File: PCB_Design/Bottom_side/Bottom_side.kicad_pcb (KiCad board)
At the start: 2 copper layers, 95.2 x 94 mm, 146 parts, among them Q1 Q_NMOS_GSD, Q2 Q_NMOS_GSD, Q3 Q_NMOS_GSD, Q4 Q_NMOS_GSD, Q5 Q_PMOS_GSD, Q6 Q_PMOS_GSD, Q7 Q_PMOS_GSD, Q8 Q_NMOS_GSD, Q9 Q_NMOS_GSD, U1 MAX668, U2 MAX668, U3 MAX668, U4 MCP4728, U5 TPS54302, U6 TPS54302

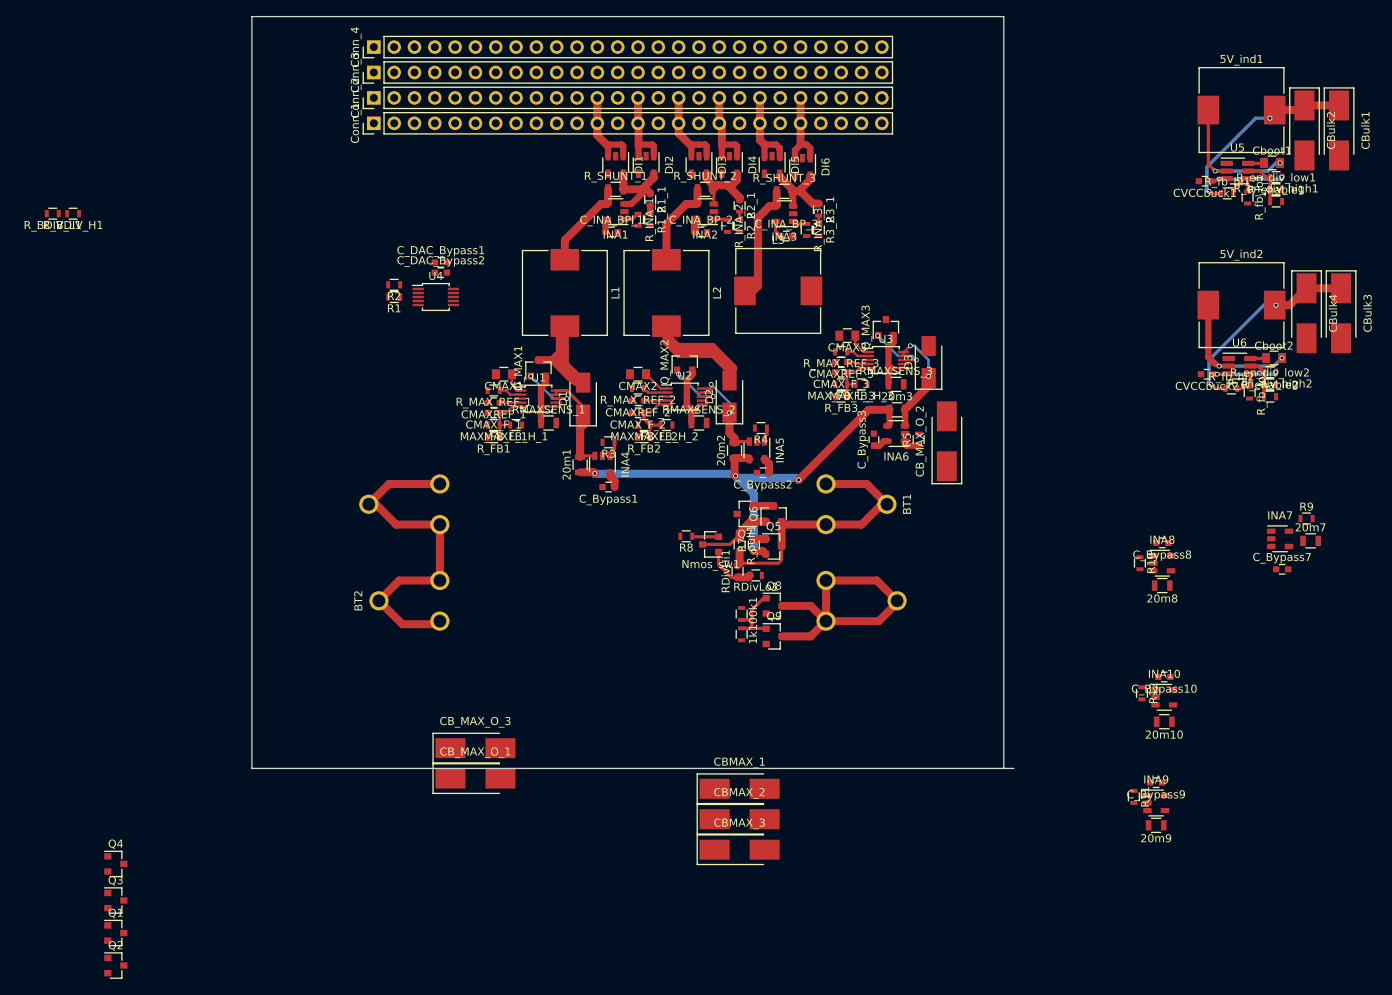
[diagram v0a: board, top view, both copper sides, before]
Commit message: PCB bottom layer populated
PCB bottom layer populated, and waiting for top layer to be merged.
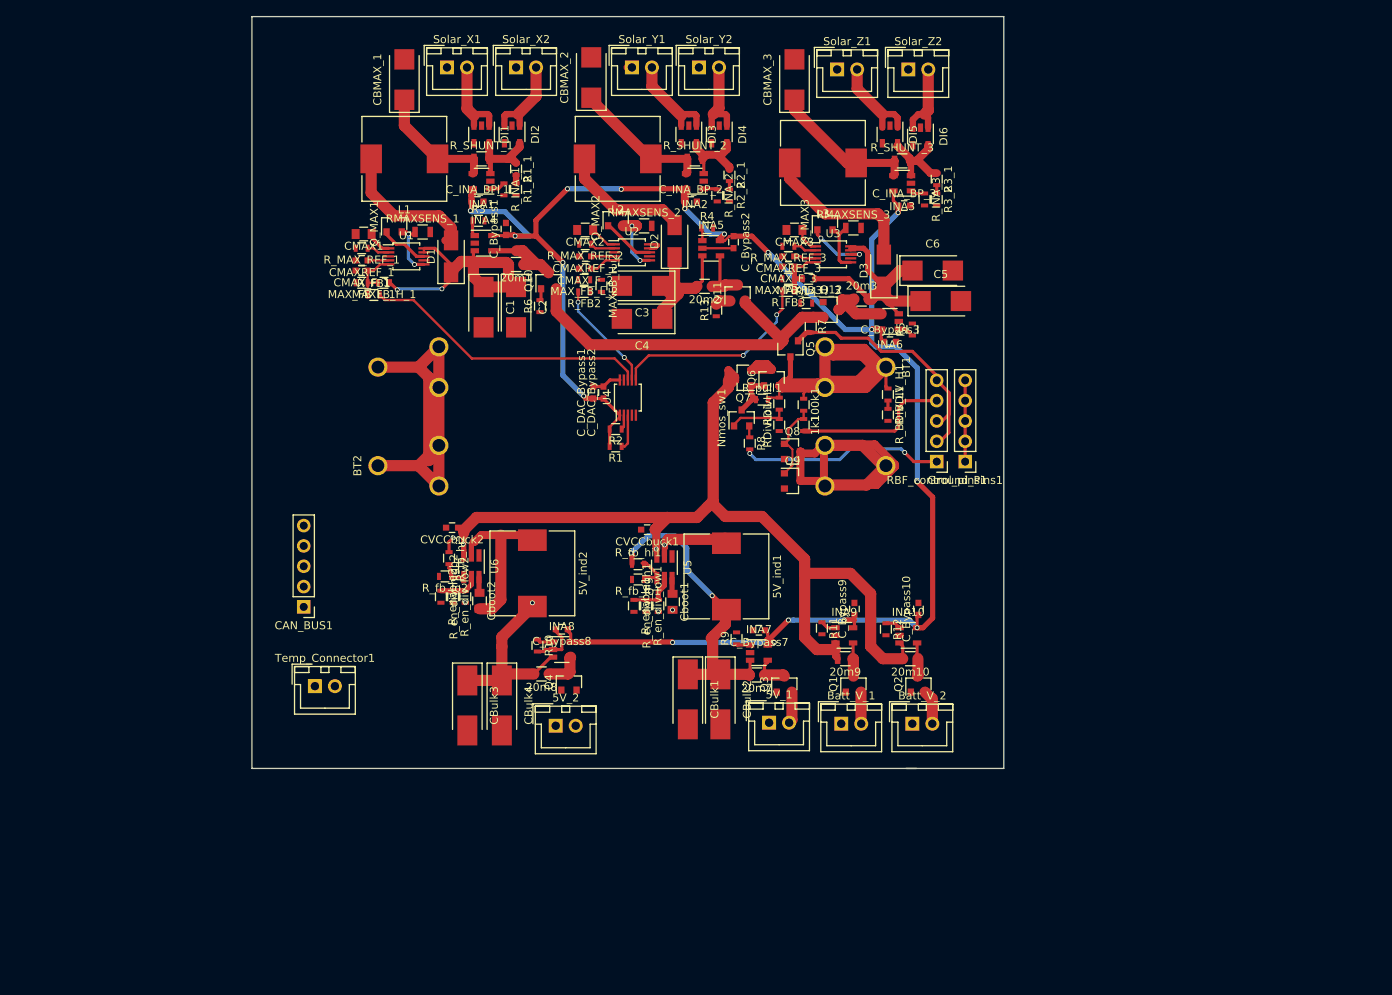
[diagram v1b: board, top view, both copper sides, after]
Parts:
- removed CB_MAX_O_1, CB_MAX_O_2, CB_MAX_O_3: 68uF, Capacitors_Tantalum_SMD:CP_Tantalum_Case-C_EIA-6032-28_Hand
- removed Conn_1, Conn_3: Conn_01x26, Socket_Strips:Socket_Strip_Straight_1x26_Pitch2.54mm
- removed Conn_2: Conn_2, Socket_Strips:Socket_Strip_Straight_1x26_Pitch2.54mm
- removed Conn_4: Conn_4, Socket_Strips:Socket_Strip_Straight_1x26_Pitch2.54mm
- added 5V_1: Jst_Conn, Connectors_JST:JST_XH_B02B-XH-A_02x2.50mm_Straight, F.Cu at (116.7, 123.8)
- added 5V_2: Jst_Conn, Connectors_JST:JST_XH_B02B-XH-A_02x2.50mm_Straight, F.Cu at (90.0, 124.2)
- added Batt_V_1: Jst_Conn, Connectors_JST:JST_XH_B02B-XH-A_02x2.50mm_Straight, F.Cu at (125.7, 124.0)
- added Batt_V_2: Jst_Conn, Connectors_JST:JST_XH_B02B-XH-A_02x2.50mm_Straight, F.Cu at (134.6, 124.0)
- added C1: CP, Capacitors_Tantalum_SMD:CP_Tantalum_Case-C_EIA-6032-28_Reflow, F.Cu at (81.0, 71.9)
- added C2: CP, Capacitors_Tantalum_SMD:CP_Tantalum_Case-C_EIA-6032-28_Reflow, F.Cu at (85.1, 71.9)
- added C3: CP, Capacitors_Tantalum_SMD:CP_Tantalum_Case-C_EIA-6032-28_Reflow, F.Cu at (100.8, 69.2)
- added C4: CP, Capacitors_Tantalum_SMD:CP_Tantalum_Case-C_EIA-6032-28_Reflow, F.Cu at (100.8, 73.3)
- added C5: CP, Capacitors_Tantalum_SMD:CP_Tantalum_Case-C_EIA-6032-28_Reflow, F.Cu at (138.2, 71.1)
- added C6: CP, Capacitors_Tantalum_SMD:CP_Tantalum_Case-C_EIA-6032-28_Reflow, F.Cu at (137.2, 67.3)
- added CAN_BUS1: 5_pin_2.56, Socket_Strips:Socket_Strip_Straight_1x05_Pitch2.54mm, F.Cu at (58.5, 109.3)
- added Ground_Pins1: 2.56_socket_male, Socket_Strips:Socket_Strip_Straight_1x05_Pitch2.54mm, F.Cu at (141.2, 91.2)
- added Q10: Q_PMOS_GSD, TO_SOT_Packages_SMD:SOT-23, F.Cu at (89.2, 68.6)
- added Q11: Q_PMOS_GSD, TO_SOT_Packages_SMD:SOT-23, F.Cu at (112.8, 70.1)
- added Q12: Q_PMOS_GSD, TO_SOT_Packages_SMD:SOT-23, F.Cu at (124.5, 72.2)
- added R13: 220k, Resistors_SMD:R_0603, F.Cu at (110.1, 72.3)
- added R14: 220k, Resistors_SMD:R_0603, F.Cu at (121.3, 71.4)
- added R6: 220k, Resistors_SMD:R_0603, F.Cu at (88.1, 71.8)
- added RBF_control_pins1: 5_pin_2.56, Socket_Strips:Socket_Strip_Straight_1x05_Pitch2.54mm, F.Cu at (137.7, 91.2)
- added Solar_X1: JST_Connector, Connectors_JST:JST_XH_B02B-XH-A_02x2.50mm_Straight, F.Cu at (76.5, 41.9)
- added Solar_X2: JST_Connector, Connectors_JST:JST_XH_B02B-XH-A_02x2.50mm_Straight, F.Cu at (85.1, 41.9)
- added Solar_Y1: JST_Connector, Connectors_JST:JST_XH_B02B-XH-A_02x2.50mm_Straight, F.Cu at (99.6, 41.9)
- added Solar_Y2: JST_Connector, Connectors_JST:JST_XH_B02B-XH-A_02x2.50mm_Straight, F.Cu at (108.0, 41.9)
- added Solar_Z1: JST_Connector, Connectors_JST:JST_XH_B02B-XH-A_02x2.50mm_Straight, F.Cu at (125.2, 42.2)
- added Solar_Z2: JST_Connector, Connectors_JST:JST_XH_B02B-XH-A_02x2.50mm_Straight, F.Cu at (134.1, 42.2)
- added Temp_Connector1: JST_conn, Connectors_JST:JST_XH_B02B-XH-A_02x2.50mm_Straight, F.Cu at (59.9, 119.3)
- BT1, BT2: footprint Batt_Hold:18650_Holder_FULL -> Battery_Holder_Lib:18650_Holder_FULL
- CBMAX_1, CBMAX_2, CBMAX_3: footprint Capacitors_Tantalum_SMD:CP_Tantalum_Case-C_EIA-6032-28_Hand -> Capacitors_Tantalum_SMD:CP_Tantalum_Case-C_EIA-6032-28_Reflow
- moved CBulk3 119.7 mm to (79.0, 121.7)
- moved CBulk4 111.9 mm to (83.3, 121.7)
- moved CBulk1 108.1 mm to (106.6, 120.9)
- moved R_BDIV_L1 107.4 mm to (131.6, 85.3), turned to 270 degrees
- moved R_enable2 106.6 mm to (75.7, 108.1), turned to 270 degrees
- moved Q2 106.3 mm to (135.4, 119.0), turned to 90 degrees
- moved R_en_div_low2 105.5 mm to (77.2, 108.1), turned to 270 degrees
- moved R_en_div_high2 104.4 mm to (78.7, 108.1), turned to 90 degrees
- moved R_BDIV_H1 104.3 mm to (131.6, 82.8), turned to 270 degrees
- moved Cboot2 103.8 mm to (80.5, 108.6), turned to 270 degrees
- moved R_fb_lo2 103.2 mm to (76.2, 105.5), turned to 180 degrees
- moved CBulk2 101.9 mm to (110.6, 120.9)
- moved R_fb_hi2 100.1 mm to (76.7, 103.3), turned to 270 degrees
- moved U6 99.2 mm to (79.5, 104.3), turned to 270 degrees
- moved CBMAX_1 98.1 mm to (71.1, 43.4), turned to 90 degrees
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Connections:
- net /Connectors/Ideal_Diodes/X+ renamed /Connectors And Inputs/Ideal_Diodes/X+
- net /Connectors/Ideal_Diodes/X- renamed /Connectors And Inputs/Ideal_Diodes/X-
- net /Connectors/Ideal_Diodes/Y+ renamed /Connectors And Inputs/Ideal_Diodes/Y+
- net /Connectors/Ideal_Diodes/Y- renamed /Connectors And Inputs/Ideal_Diodes/Y-
- net /Connectors/Ideal_Diodes/Z+ renamed /Connectors And Inputs/Ideal_Diodes/Z+
- net /Connectors/Ideal_Diodes/Z- renamed /Connectors And Inputs/Ideal_Diodes/Z-
- net /Input/InaOutput/INA_out/Ina_Analog renamed /Input/InaOutput/INA_out_2/Ina_Analog
- net /Input/LDAC renamed /LDAC
- net /Input/SCL renamed /SCL
- net /Input/SDA renamed /SDA
- 20m1 pad 1: /Input/Output_1 -> /Input/InaOutput/INA_out/I_out
- 20m10 pad 1: /OUTPUT/Sheet5A5E5DCD/I_out -> /OUTPUT/INA_BV_2/I_out
- 20m2 pad 1: /Input/Output_1 -> /Input/InaOutput/INA_out_2/I_out
- 20m3 pad 1: /Input/Output_1 -> /Input/InaOutput/INA_out_3/I_out
- 20m7 pad 1: /OUTPUT/Sheet5A5E5DCD/I_out -> /OUTPUT/Ina_5V_Out/I_out
- 20m7 pad 2: /OUTPUT/5VBuck/5V_OUT -> /OUTPUT/5VBuck1/5V_OUT
- 20m8 pad 1: /OUTPUT/Sheet5A5E5DCD/I_out -> /OUTPUT/Ina_3V6_Out/I_out
- 20m8 pad 2: /OUTPUT/5VBuck/5V_OUT -> /OUTPUT/5VBuck2/5V_OUT
- 20m9 pad 1: /OUTPUT/Sheet5A5E5DCD/I_out -> /OUTPUT/Ina_BV_1/I_out
- 5V_ind1 pad 2: /OUTPUT/5VBuck/5V_OUT -> /OUTPUT/5VBuck1/5V_OUT
- 5V_ind2 pad 2: /OUTPUT/5VBuck/5V_OUT -> /OUTPUT/5VBuck2/5V_OUT
- CBulk1 pad 1: /OUTPUT/5VBuck/5V_OUT -> /OUTPUT/5VBuck1/5V_OUT
- CBulk2 pad 1: /OUTPUT/5VBuck/5V_OUT -> /OUTPUT/5VBuck1/5V_OUT
- CBulk3 pad 1: /OUTPUT/5VBuck/5V_OUT -> /OUTPUT/5VBuck2/5V_OUT
- CBulk4 pad 1: /OUTPUT/5VBuck/5V_OUT -> /OUTPUT/5VBuck2/5V_OUT
- CMAX_F_2 pad 1: /Input/Boost_Converters/MAX668/FB -> /Input/Boost_Converters/MAX668_2/FB
- CMAX_F_3 pad 1: /Input/Boost_Converters/MAX668/FB -> /Input/Boost_Converters/MAX668_3/FB
- INA10 pad 4: /OUTPUT/Sheet5A5E5DCD/I_out -> /OUTPUT/INA_BV_2/I_out
- INA4 pad 4: /Input/Output_1 -> /Input/InaOutput/INA_out/I_out
- INA5 pad 4: /Input/Output_1 -> /Input/InaOutput/INA_out_2/I_out
- INA6 pad 4: /Input/Output_1 -> /Input/InaOutput/INA_out_3/I_out
- INA7 pad 3: /OUTPUT/5VBuck/5V_OUT -> /OUTPUT/5VBuck1/5V_OUT
- INA7 pad 4: /OUTPUT/Sheet5A5E5DCD/I_out -> /OUTPUT/Ina_5V_Out/I_out
- INA8 pad 3: /OUTPUT/5VBuck/5V_OUT -> /OUTPUT/5VBuck2/5V_OUT
- INA8 pad 4: /OUTPUT/Sheet5A5E5DCD/I_out -> /OUTPUT/Ina_3V6_Out/I_out
- INA9 pad 4: /OUTPUT/Sheet5A5E5DCD/I_out -> /OUTPUT/Ina_BV_1/I_out
- MAXFB_H_2 pad 2: /Input/Boost_Converters/MAX668/FB -> /Input/Boost_Converters/MAX668_2/FB
- MAXFB_H_3 pad 2: /Input/Boost_Converters/MAX668/FB -> /Input/Boost_Converters/MAX668_3/FB
- MAX_FB_L_2 pad 1: /Input/Boost_Converters/MAX668/FB -> /Input/Boost_Converters/MAX668_2/FB
- MAX_FB_L_3 pad 1: /Input/Boost_Converters/MAX668/FB -> /Input/Boost_Converters/MAX668_3/FB
- Q1 pad 3: /OUTPUT/Sheet5A5E5DCD/I_out -> /OUTPUT/Ina_BV_1/I_out
- Q2 pad 2: Net-(Q2-Pad2) -> /Batt_V_2
- Q2 pad 3: /OUTPUT/Sheet5A5E5DCD/I_out -> /OUTPUT/INA_BV_2/I_out
- Q3 pad 3: /OUTPUT/Sheet5A5E5DCD/I_out -> /OUTPUT/Ina_5V_Out/I_out
- Q4 pad 3: /OUTPUT/Sheet5A5E5DCD/I_out -> /OUTPUT/Ina_3V6_Out/I_out
- R_BDIV_H1 pad 1: /Input/Output_1 -> Battery_+
- R_FB2 pad 1: /Input/Boost_Converters/MAX668/FB -> /Input/Boost_Converters/MAX668_2/FB
- R_FB3 pad 1: /Input/Boost_Converters/MAX668/FB -> /Input/Boost_Converters/MAX668_3/FB
- R_fb_hi1 pad 1: /OUTPUT/5VBuck/5V_OUT -> /OUTPUT/5VBuck1/5V_OUT
- R_fb_hi2 pad 1: /OUTPUT/5VBuck/5V_OUT -> /OUTPUT/5VBuck2/5V_OUT
- U2 pad 5: /Input/Boost_Converters/MAX668/FB -> /Input/Boost_Converters/MAX668_2/FB
- U3 pad 5: /Input/Boost_Converters/MAX668/FB -> /Input/Boost_Converters/MAX668_3/FB
- U4 pad 6: /Input/DAC/Dac_1 -> /Input/DAC/Dac_3
- U4 pad 8: /Input/DAC/Dac_3 -> /Input/DAC/Dac_1
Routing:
- net (no net): track 0.00 -> 652.8 mm, vias 0 -> 14
- net /3V3: track 11.2 -> 228.2 mm, vias 0 -> 17
- net /OUTPUT/POWER_INPUT: track 19.5 -> 137.4 mm
- net /Input/Output_1: track 60.9 -> 0.00 mm, vias 4 -> 0
- net /OUTPUT/5VBuck/5V_OUT: track 50.5 -> 0.00 mm, vias 4 -> 0
- net /OUTPUT/5VBuck2/5V_OUT: track 0.00 -> 39.6 mm, vias 0 -> 2
- net Battery_+: track 35.6 -> 72.3 mm
- net RBF1: track 1.48 -> 32.0 mm
- net Net-(D1-Pad2): track 26.9 -> 0.00 mm
- net RBF2: track 0.00 -> 25.4 mm, vias 0 -> 2
- net Net-(D2-Pad2): track 25.1 -> 0.00 mm
- net /Input/Boost_Converters/MAX668/FB: track 22.2 -> 0.00 mm
- net GND_DSW: track 0.00 -> 20.4 mm
- net Net-(5V_ind2-Pad1): track 18.2 -> 0.00 mm, vias 2 -> 0
- net Battery_-: track 37.6 -> 52.8 mm
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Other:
- board size 95.2 x 94 mm -> 94 x 94 mm
- copper layers 2 -> 4
- net class Default: clearance 0.15 -> 0.1
- rule trace_clearance: 0.15 -> 0.1
